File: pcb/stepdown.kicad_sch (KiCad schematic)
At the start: 15 parts, among them U1 SY8286ARAC

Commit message: pcb: exploration
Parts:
- L1: value YNR6045-470M -> 3u3; footprint Inductor_SMD:L_Taiyo-Yuden_NR-60xx -> Inductor_SMD:L_Sunlord_MWSA0503S; JLCPN (none) -> C325963
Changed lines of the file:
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@@
 			)
 		)
-		(property "Value" "YNR6045-470M"
-			(at 179.07 53.848 90)
+		(property "Value" "3u3"
+			(at 177.546 54.102 90)
 			(effects
 				(font
@@
 			)
 		)
-		(property "Footprint" "Inductor_SMD:L_Taiyo-Yuden_NR-60xx"
+		(property "Footprint" "Inductor_SMD:L_Sunlord_MWSA0503S"
 			(at 177.546 64.77 90)
 			(effects
@@
 			)
 		)
-		(property "Datasheet" ""
+		(property "Datasheet" "https://www.lcsc.com/datasheet/lcsc_datasheet_2409271703_Sunltech-Tech-SLO0530H3R3MTT_C325963.pdf"
 			(at 179.07 59.69 0)
 			(effects
@@
 					(size 1.524 1.524)
 				)
+				(hide yes)
 			)
 		)
-		(property "Description" "10 uH, 2 A"
+		(property "Description" "3.3 uH, 5 A"
 			(at 179.07 59.69 0)
 			(effects
@@
 				)
 				(hide yes)
+			)
+		)
+		(property "JLCPN" "C325963"
+			(at 179.07 59.69 90)
+			(effects
+				(font
+					(size 1.524 1.524)
+				)
+				(hide yes)

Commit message: initial routing done
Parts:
- L1: value 3u3 -> SMDRH104R-4R7NT; footprint Inductor_SMD:L_Sunlord_MWSA0503S -> espirgbani:SMDRH104R-4R7NT; JLCPN C325963 -> C44850
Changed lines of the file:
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@@
 			)
 		)
-		(property "Value" "3u3"
+		(property "Value" "SMDRH104R-4R7NT"
 			(at 177.546 54.102 90)
 			(effects
@@
 			)
 		)
-		(property "Footprint" "Inductor_SMD:L_Sunlord_MWSA0503S"
+		(property "Footprint" "espirgbani:SMDRH104R-4R7NT"
 			(at 177.546 64.77 90)
 			(effects
@@
 			)
 		)
-		(property "Description" "3.3 uH, 5 A"
+		(property "Description" " 5.4A 4.7uH Shielded inductor ±20% 7A SMD,10.4x10.3mm Power Inductors ROHS"
 			(at 179.07 59.69 0)
 			(effects
@@
 			)
 		)
-		(property "JLCPN" "C325963"
+		(property "JLCPN" "C44850"
 			(at 179.07 59.69 90)
 			(effects

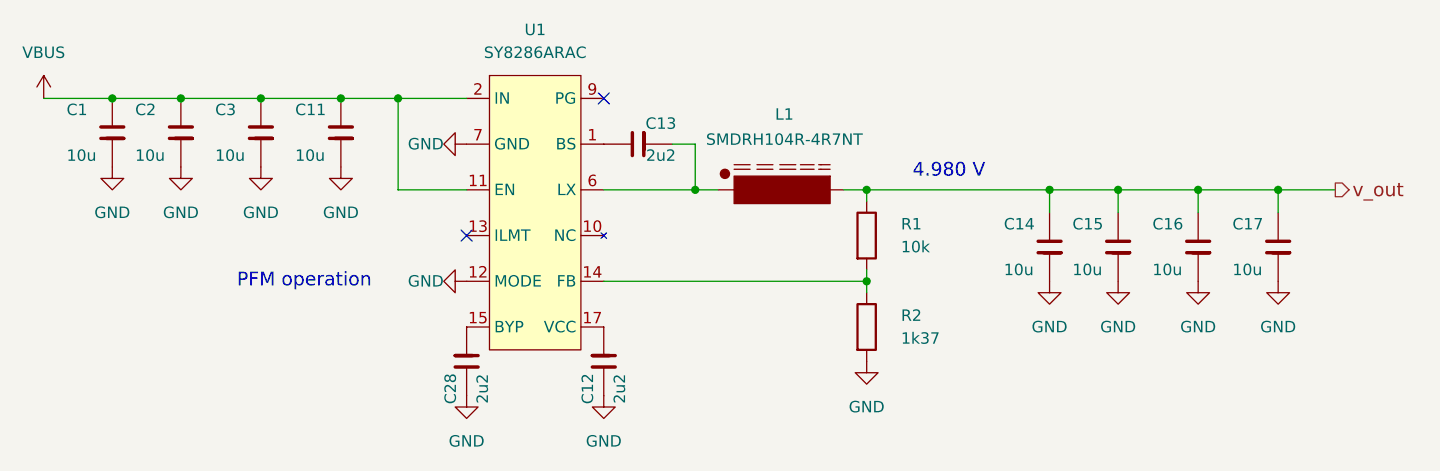
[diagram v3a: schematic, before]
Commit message: put a cool pattern on the bottom silk
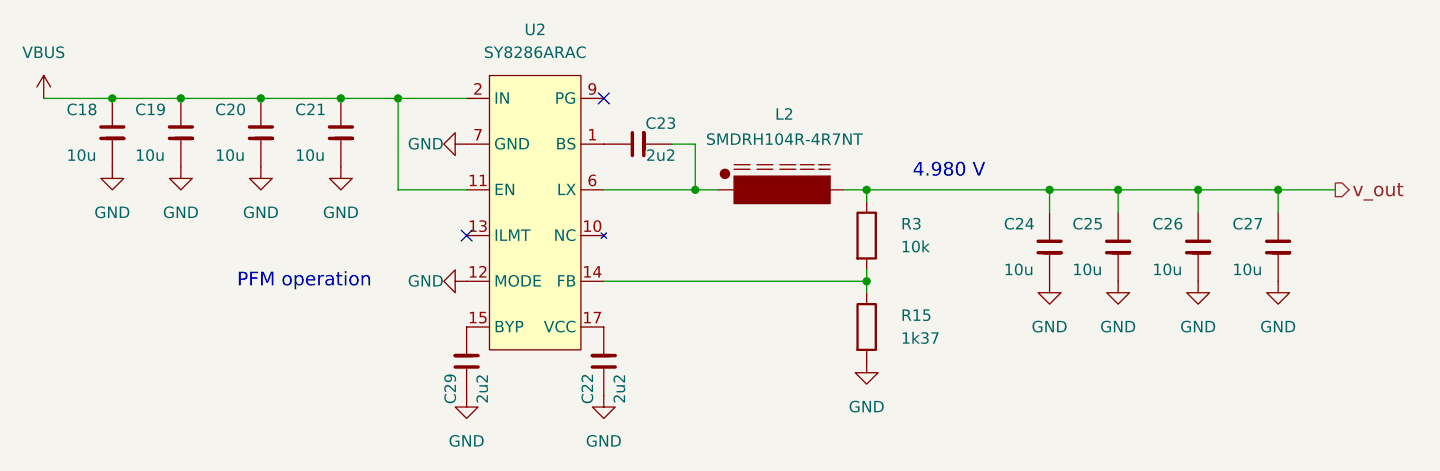
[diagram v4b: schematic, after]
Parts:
- renumbered C1 to C18, C2 to C19, C3 to C20, C11 to C21, C12 to C22, C13 to C23, C14 to C24, C15 to C25, C16 to C26, C17 to C27, C28 to C29, L1 to L2, R2 to R15, R1 to R3, U1 to U2
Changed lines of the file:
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@@
 		(dnp no)
 		(fields_autoplaced yes)
-		(property "Reference" "#PWR018"
+		(property "Reference" "#PWR056"
 			(at 128.27 63.5 0)
 			(effects
@@
 		(on_board yes)
 		(dnp no)
-		(property "Reference" "C11"
+		(property "Reference" "C21"
 			(at 123.19 50.8 90)
 			(effects
@@
 		(dnp no)
 		(fields_autoplaced yes)
-		(property "Reference" "#PWR05"
+		(property "Reference" "#PWR053"
 			(at 102.87 63.5 0)
 			(effects
@@
 		(dnp no)
 		(fields_autoplaced yes)
-		(property "Reference" "#PWR068"
+		(property "Reference" "#PWR069"
 			(at 142.24 88.9 0)
 			(effects
@@
 		(dnp no)
 		(fields_autoplaced yes)
-		(property "Reference" "#PWR010"
+		(property "Reference" "#PWR063"
 			(at 223.52 76.2 0)
 			(effects
@@
 		(dnp no)
 		(fields_autoplaced yes)
-		(property "Reference" "U1"
+		(property "Reference" "U2"
 			(at 149.86 41.91 0)
 			(effects
@@
 		(on_board yes)
 		(dnp no)
-		(property "Reference" "C17"
+		(property "Reference" "C27"
 			(at 227.33 63.5 90)
 			(effects
@@
 		(on_board yes)
 		(dnp no)
-		(property "Reference" "C28"
+		(property "Reference" "C29"
 			(at 140.462 81.788 0)
 			(effects
@@
 		(on_board yes)
 		(dnp no)
-		(property "Reference" "C1"
+		(property "Reference" "C18"
 			(at 97.79 50.8 90)
 			(effects
@@
 		(dnp no)
 		(fields_autoplaced yes)
-		(property "Reference" "#PWR06"
+		(property "Reference" "#PWR062"
 			(at 214.63 76.2 0)
 			(effects
@@
 		(on_board yes)
 		(dnp no)
-		(property "Reference" "C16"
+		(property "Reference" "C26"
 			(at 218.44 63.5 90)
 			(effects
@@
 		(on_board yes)
 		(dnp no)
-		(property "Reference" "C3"
+		(property "Reference" "C20"
 			(at 114.3 50.8 90)
 			(effects
@@
 		(on_board yes)
 		(dnp no)
-		(property "Reference" "C2"
+		(property "Reference" "C19"
 			(at 105.41 50.8 90)
 			(effects
@@
 		(dnp no)
 		(fields_autoplaced yes)
-		(property "Reference" "#PWR014"
+		(property "Reference" "#PWR064"
 			(at 232.41 76.2 0)
 			(effects
@@
 		(dnp no)
 		(fields_autoplaced yes)
-		(property "Reference" "#PWR08"
+		(property "Reference" "#PWR057"
 			(at 135.89 54.61 0)
 			(effects
@@
 		(on_board yes)
 		(dnp no)
-		(property "Reference" "C12"
+		(property "Reference" "C22"
 			(at 155.702 81.788 0)
 			(effects
@@
 		(dnp no)
 		(fields_autoplaced yes)
-		(property "Reference" "R1"
+		(property "Reference" "R3"
 			(at 190.5 63.4999 0)
 			(effects
@@
 		(dnp no)
 		(fields_autoplaced yes)
-		(property "Reference" "#PWR09"
+		(property "Reference" "#PWR058"
 			(at 135.89 69.85 0)
 			(effects
@@
 		(dnp no)
 		(fields_autoplaced yes)
-		(property "Reference" "#PWR026"
+		(property "Reference" "#PWR060"
 			(at 186.69 85.09 0)
 			(effects
@@
 		(dnp no)
 		(fields_autoplaced yes)
-		(property "Reference" "#PWR051"
+		(property "Reference" "#PWR052"
 			(at 95.25 53.34 0)
 			(effects
@@
 		(on_board yes)
 		(dnp no)
-		(property "Reference" "L1"
+		(property "Reference" "L2"
 			(at 177.546 51.308 90)
 			(effects
@@
 		(on_board yes)
 		(dnp no)
-		(property "Reference" "R2"
+		(property "Reference" "R15"
 			(at 190.5 73.6599 0)
 			(effects
@@
 		(dnp no)
 		(fields_autoplaced yes)
-		(property "Reference" "#PWR07"
+		(property "Reference" "#PWR054"
 			(at 110.49 63.5 0)
 			(effects
@@
 		(on_board yes)
 		(dnp no)
-		(property "Reference" "C15"
+		(property "Reference" "C25"
 			(at 209.55 63.5 90)
 			(effects
@@
 		(dnp no)
 		(fields_autoplaced yes)
-		(property "Reference" "#PWR011"
+		(property "Reference" "#PWR055"
 			(at 119.38 63.5 0)
 			(effects
@@
 		(dnp no)
 		(fields_autoplaced yes)
-		(property "Reference" "#PWR04"
+		(property "Reference" "#PWR061"
 			(at 207.01 76.2 0)
 			(effects
@@
 		(dnp no)
 		(fields_autoplaced yes)
-		(property "Reference" "#PWR025"
+		(property "Reference" "#PWR059"
 			(at 157.48 88.9 0)
 			(effects
@@
 		(on_board yes)
 		(dnp no)
-		(property "Reference" "C14"
+		(property "Reference" "C24"
 			(at 201.93 63.5 90)
 			(effects
@@
 		(on_board yes)
 		(dnp no)
-		(property "Reference" "C13"
+		(property "Reference" "C23"
 			(at 163.83 52.324 0)
 			(effects

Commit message: first sketch of optimized pinout
Support SD MMC mode x4
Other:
- title: (none) -> ESP Pinball RGB Animation clock (espirgbani)
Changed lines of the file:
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@@
 	(paper "A4")
 	(title_block
-		(date "2024-10-19")
-		(rev "2")
+		(title "ESP Pinball RGB Animation clock (espirgbani)")
+		(date "2025-01-14")
+		(rev "3")
 	)
 	(junction

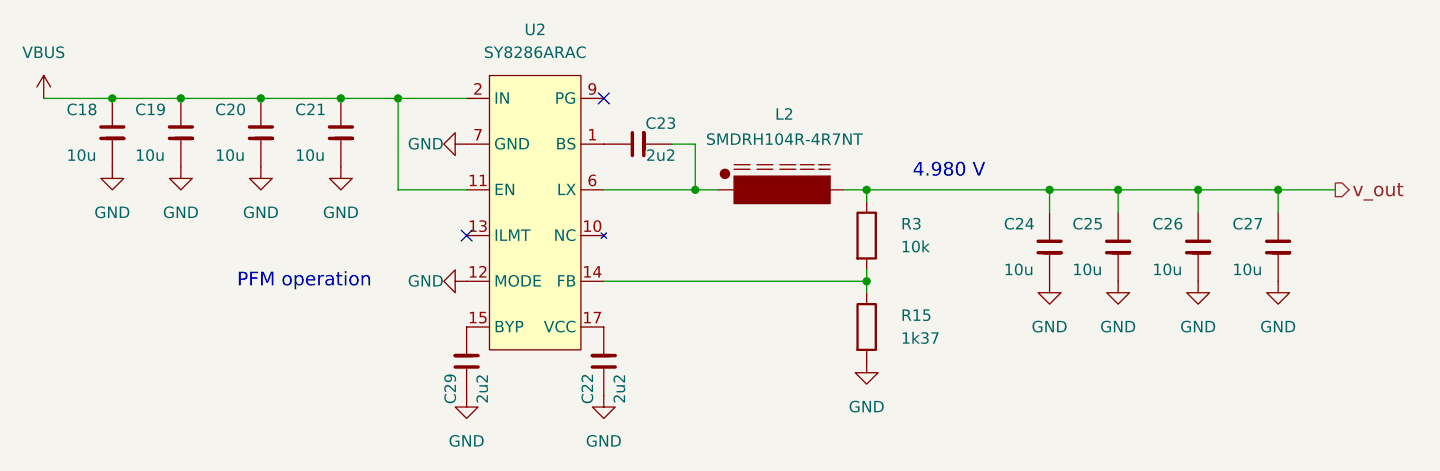
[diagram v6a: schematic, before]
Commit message: pcb: add some items to the TODO list
  * detect 5 V operation with ADC
  * IR receiver
  * RTC chip
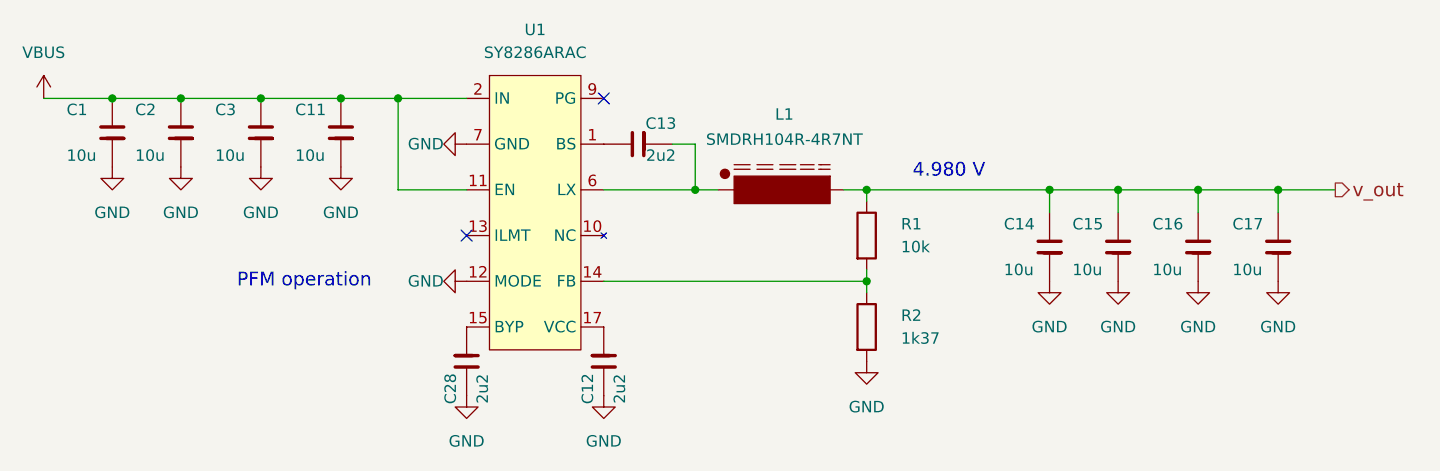
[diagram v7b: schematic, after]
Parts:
- renumbered C18 to C1, C21 to C11, C22 to C12, C23 to C13, C24 to C14, C25 to C15, C26 to C16, C27 to C17, C19 to C2, C29 to C28, C20 to C3, L2 to L1, R3 to R1, R15 to R2, U2 to U1
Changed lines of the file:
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@@
 (kicad_sch
-	(version 20231120)
+	(version 20250114)
 	(generator "eeschema")
-	(generator_version "8.0")
+	(generator_version "9.0")
 	(paper "A4")
 	(title_block
@@
 		(rev "3")
 	)
+	(text "4.980 V"
+		(exclude_from_sim no)
+		(at 195.834 57.658 0)
+		(effects
+			(font
+				(size 1.524 1.524)
+			)
+		)
+	)
+	(text "PFM operation"
+		(exclude_from_sim no)
+		(at 124.206 69.85 0)
+		(effects
+			(font
+				(size 1.524 1.524)
+			)
+		)
+	)
 	(junction
 		(at 128.27 49.53)
@@
 		)
 	)
-	(text "4.980 V"
-		(exclude_from_sim no)
-		(at 195.834 57.658 0)
+	(hierarchical_label "v_out"
+		(shape output)
+		(at 238.76 59.69 0)
 		(effects
 			(font
 				(size 1.524 1.524)
 			)
-		)
-	)
-	(text "PFM operation"
-		(exclude_from_sim no)
-		(at 124.206 69.85 0)
-		(effects
-			(font
-				(size 1.524 1.524)
-			)
-		)
-	)
-	(hierarchical_label "v_out"
-		(shape output)
-		(at 238.76 59.69 0)
-		(fields_autoplaced yes)
-		(effects
-			(font
-				(size 1.524 1.524)
-			)
 			(justify left)
 		)
@@
 		(dnp no)
 		(fields_autoplaced yes)
-		(property "Reference" "#PWR056"
+		(property "Reference" "#PWR018"
 			(at 128.27 63.5 0)
 			(effects
@@
 		(on_board yes)
 		(dnp no)
-		(property "Reference" "C21"
+		(property "Reference" "C11"
 			(at 123.19 50.8 90)
 			(effects
@@
 		(dnp no)
 		(fields_autoplaced yes)
-		(property "Reference" "#PWR053"
+		(property "Reference" "#PWR05"
 			(at 102.87 63.5 0)
 			(effects
@@
 		(dnp no)
 		(fields_autoplaced yes)
-		(property "Reference" "#PWR069"
+		(property "Reference" "#PWR068"
 			(at 142.24 88.9 0)
 			(effects
@@
 		(dnp no)
 		(fields_autoplaced yes)
-		(property "Reference" "#PWR063"
+		(property "Reference" "#PWR010"
 			(at 223.52 76.2 0)
 			(effects
@@
 		(dnp no)
 		(fields_autoplaced yes)
-		(property "Reference" "U2"
+		(property "Reference" "U1"
 			(at 149.86 41.91 0)
 			(effects
@@
 		(on_board yes)
 		(dnp no)
-		(property "Reference" "C27"
+		(property "Reference" "C17"
 			(at 227.33 63.5 90)
 			(effects
@@
 		(on_board yes)
 		(dnp no)
-		(property "Reference" "C29"
+		(property "Reference" "C28"
 			(at 140.462 81.788 0)
 			(effects
@@
 		(on_board yes)
 		(dnp no)
-		(property "Reference" "C18"
+		(property "Reference" "C1"
 			(at 97.79 50.8 90)
 			(effects
@@
 		(dnp no)
 		(fields_autoplaced yes)
-		(property "Reference" "#PWR062"
+		(property "Reference" "#PWR06"
 			(at 214.63 76.2 0)
 			(effects
@@
 		(on_board yes)
 		(dnp no)
-		(property "Reference" "C26"
+		(property "Reference" "C16"
 			(at 218.44 63.5 90)
 			(effects
@@
 		(on_board yes)
 		(dnp no)
-		(property "Reference" "C20"
+		(property "Reference" "C3"
 			(at 114.3 50.8 90)
 			(effects
@@
 		(on_board yes)
 		(dnp no)
-		(property "Reference" "C19"
+		(property "Reference" "C2"
 			(at 105.41 50.8 90)
 			(effects
@@
 		(dnp no)
 		(fields_autoplaced yes)
-		(property "Reference" "#PWR064"
+		(property "Reference" "#PWR014"
 			(at 232.41 76.2 0)
 			(effects
@@
 		(dnp no)
 		(fields_autoplaced yes)
-		(property "Reference" "#PWR057"
+		(property "Reference" "#PWR08"
 			(at 135.89 54.61 0)
 			(effects
@@
 		(on_board yes)
 		(dnp no)
-		(property "Reference" "C22"
+		(property "Reference" "C12"
 			(at 155.702 81.788 0)
 			(effects
@@
 		(dnp no)
 		(fields_autoplaced yes)
-		(property "Reference" "R3"
+		(property "Reference" "R1"
 			(at 190.5 63.4999 0)
 			(effects
@@
 		(dnp no)
 		(fields_autoplaced yes)
-		(property "Reference" "#PWR058"
+		(property "Reference" "#PWR09"
 			(at 135.89 69.85 0)
 			(effects
@@
 		(dnp no)
 		(fields_autoplaced yes)
-		(property "Reference" "#PWR060"
+		(property "Reference" "#PWR026"
 			(at 186.69 85.09 0)
 			(effects
@@
 		(dnp no)
 		(fields_autoplaced yes)
-		(property "Reference" "#PWR052"
+		(property "Reference" "#PWR051"
 			(at 95.25 53.34 0)
 			(effects
@@
 		(on_board yes)
 		(dnp no)
-		(property "Reference" "L2"
+		(property "Reference" "L1"
 			(at 177.546 51.308 90)
 			(effects
@@
 		(on_board yes)
 		(dnp no)
-		(property "Reference" "R15"
+		(property "Reference" "R2"
 			(at 190.5 73.6599 0)
 			(effects
@@
 		(dnp no)
 		(fields_autoplaced yes)
-		(property "Reference" "#PWR054"
+		(property "Reference" "#PWR07"
 			(at 110.49 63.5 0)
 			(effects
@@
 		(on_board yes)
 		(dnp no)
-		(property "Reference" "C25"
+		(property "Reference" "C15"
 			(at 209.55 63.5 90)
 			(effects
@@
 		(dnp no)
 		(fields_autoplaced yes)
-		(property "Reference" "#PWR055"
+		(property "Reference" "#PWR011"
 			(at 119.38 63.5 0)
 			(effects
@@
 		(dnp no)
 		(fields_autoplaced yes)
-		(property "Reference" "#PWR061"
+		(property "Reference" "#PWR04"
 			(at 207.01 76.2 0)
 			(effects
@@
 		(dnp no)
 		(fields_autoplaced yes)
-		(property "Reference" "#PWR059"
+		(property "Reference" "#PWR025"
 			(at 157.48 88.9 0)
 			(effects
@@
 		(on_board yes)
 		(dnp no)
-		(property "Reference" "C24"
+		(property "Reference" "C14"
 			(at 201.93 63.5 90)
 			(effects
@@
 		(on_board yes)
 		(dnp no)
-		(property "Reference" "C23"
+		(property "Reference" "C13"
 			(at 163.83 52.324 0)
 			(effects
